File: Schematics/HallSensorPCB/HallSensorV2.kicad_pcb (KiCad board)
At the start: 2 copper layers, 3 parts, among them J1 Conn_02x03_Counter_Clockwise, J2 Conn_01x04_Pin

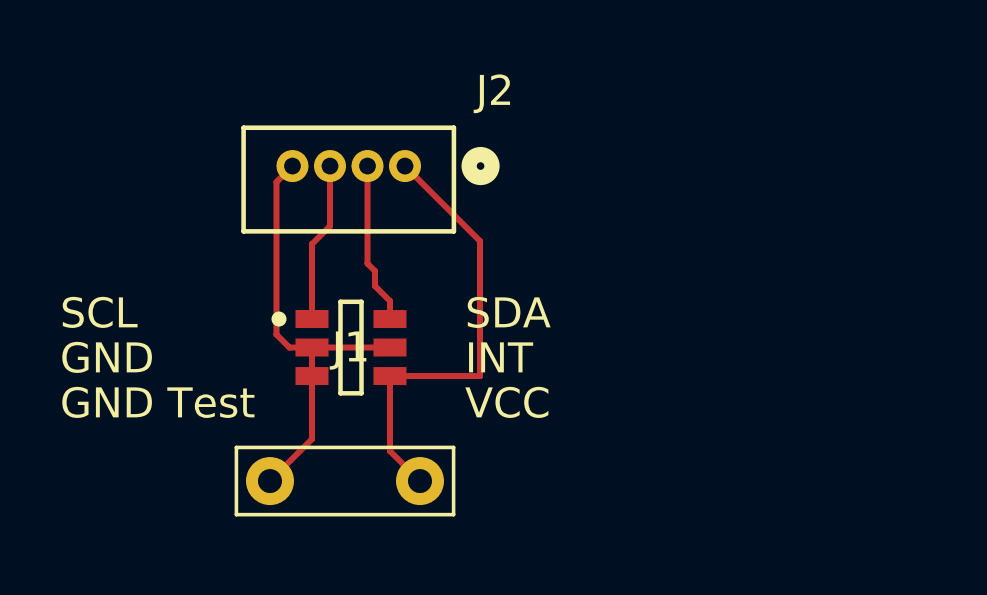
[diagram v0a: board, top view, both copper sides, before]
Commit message: Update hall schematic and pcb  - add exact sensor schematic, models, etc  - rerouted traces
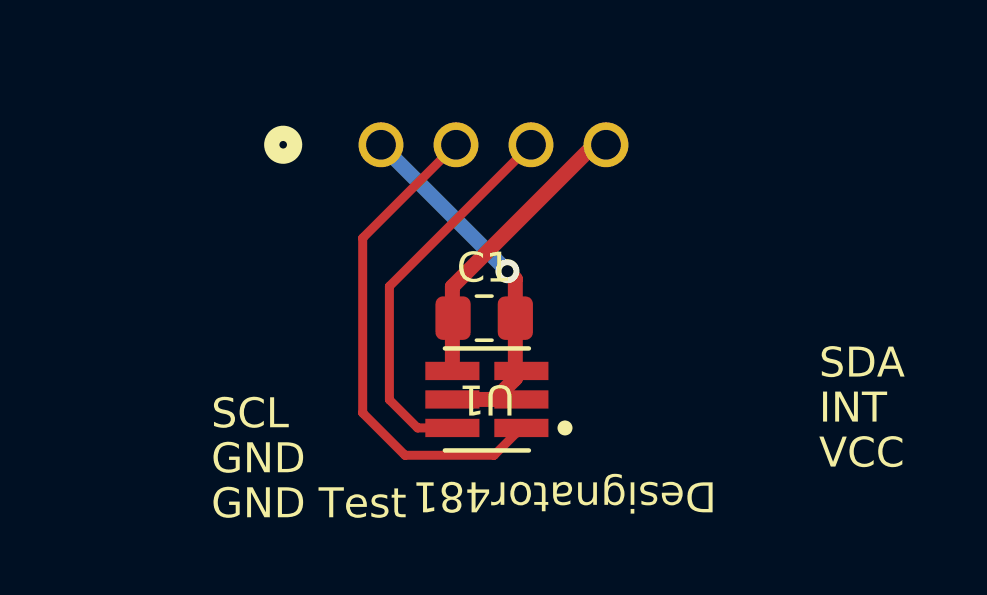
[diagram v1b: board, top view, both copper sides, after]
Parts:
- removed J1: Conn_02x03_Counter_Clockwise, footprints:DBV0006A-MFG
- added U1: TMAG5273A1QDBVT, TMAG5273A1QDBVT:DBV0006A-IPC_A, F.Cu at (49.2, 40.3)
- C1: footprint Capacitor_THT:C_Rect_L7.0mm_W2.0mm_P5.00mm -> Capacitor_SMD:C_0805_2012Metric_Pad1.18x1.45mm_HandSolder
- J2: footprint footprintsconn4:CONN04_530470460_MOL -> B04B_XASK_1:CONN_B04B-XASK-1_JST; moved to B.Cu
- moved C1 8.97 mm to (49.1, 37.6)
- moved J2 1.07 mm to (45.7, 31.8), turned to 180 degrees
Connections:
- C1 pad 1: GND -> +3V3
- C1 pad 2: Net-(J1-Pin_4) -> GND
- J2 pad 1: Net-(J1-Pin_4) -> GND
- J2 pad 2: Net-(J1-Pin_6) -> SCL
- J2 pad 3: Net-(J1-Pin_1) -> SCA
- J2 pad 4: GND -> +3V3
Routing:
- net SCL: track 0.00 -> 16.5 mm
- net Net-(J1-Pin_4): track 14.9 -> 0.00 mm
- net SCA: track 0.00 -> 12.9 mm
- net +3V3: track 0.00 -> 9.89 mm
- net Net-(J1-Pin_6): track 5.41 -> 0.00 mm
- net Net-(J1-Pin_1): track 5.35 -> 0.00 mm
- net GND: track 14.8 -> 12.0 mm, vias 0 -> 1
